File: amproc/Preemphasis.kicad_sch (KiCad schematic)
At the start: 30 parts

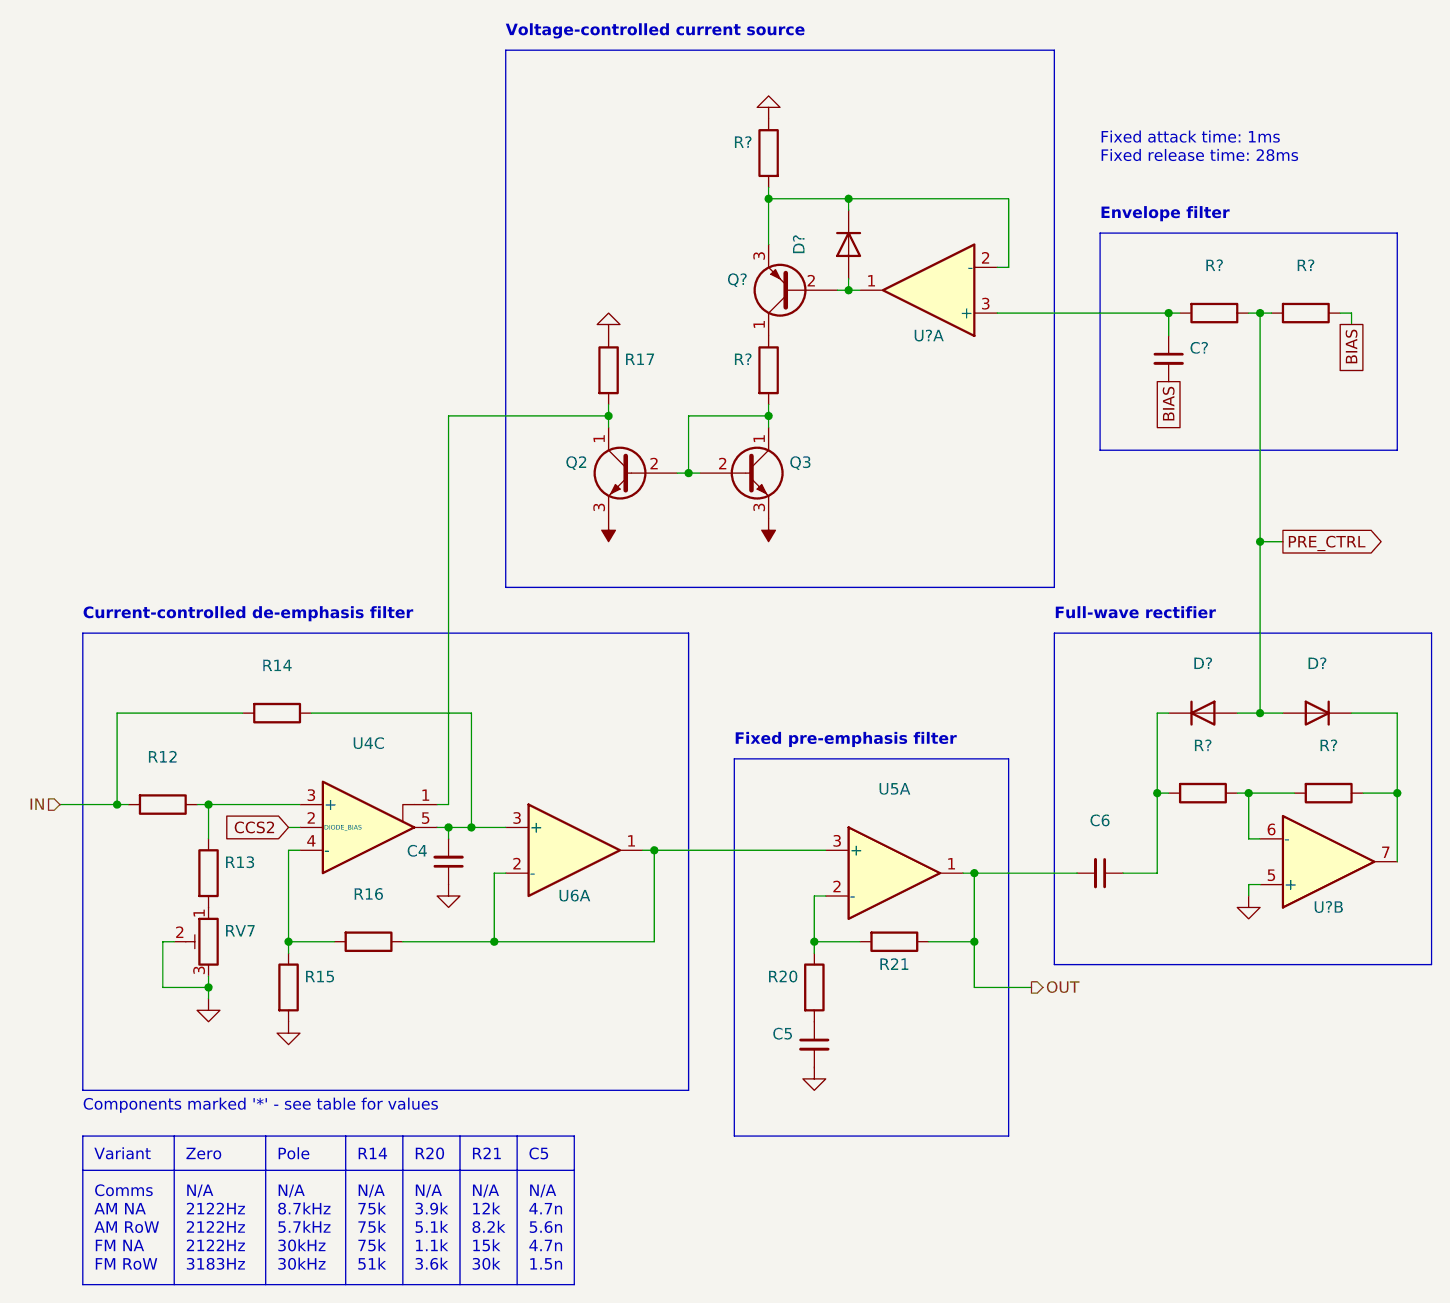
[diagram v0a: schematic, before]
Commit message: Fix U8, U9 pinouts
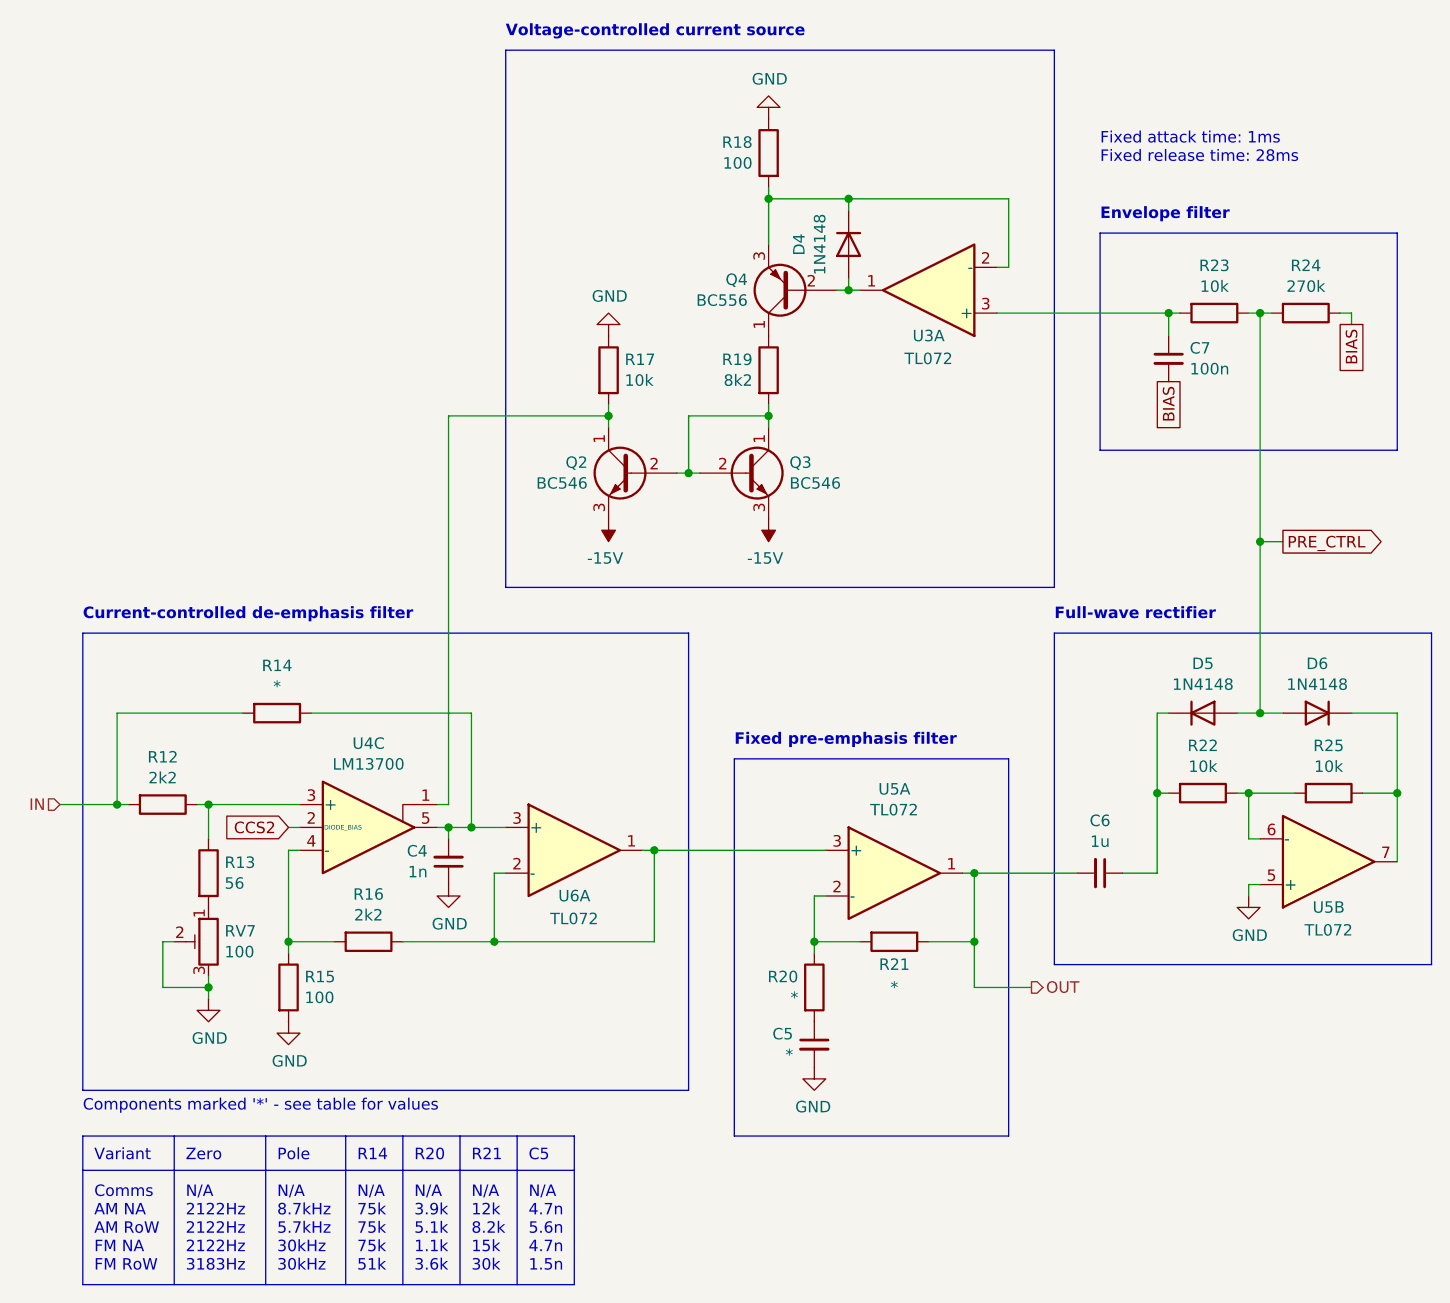
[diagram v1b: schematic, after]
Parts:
- C4: value (none) -> 1n; footprint (none) -> Capacitors_THT:C_Rect_L7.2mm_W2.5mm_P5.00mm_FKS2_FKP2_MKS2_MKP2
- C5: value (none) -> *; footprint (none) -> Capacitors_THT:C_Rect_L7.2mm_W2.5mm_P5.00mm_FKS2_FKP2_MKS2_MKP2
- C6: value (none) -> 1u; footprint (none) -> Capacitors_THT:C_Rect_L7.2mm_W5.5mm_P5.00mm_FKS2_FKP2_MKS2_MKP2
- C7: renamed from C?; value (none) -> 100n; footprint (none) -> Capacitors_THT:C_Rect_L7.2mm_W2.5mm_P5.00mm_FKS2_FKP2_MKS2_MKP2
- D4, D5, D6: renamed from D?; value (none) -> 1N4148; footprint (none) -> Diodes_THT:D_DO-35_SOD27_P7.62mm_Horizontal
- Q2, Q3: value (none) -> BC546; footprint (none) -> TO_SOT_Packages_THT:TO-92_Inline_Narrow_Oval
- Q4: renamed from Q?; value (none) -> BC556; footprint (none) -> TO_SOT_Packages_THT:TO-92_Inline_Narrow_Oval
- R12, R16: value (none) -> 2k2; footprint (none) -> amproc:R_Axial_DIN0207_L6.3mm_D2.5mm_P7.62mm_Horizontal_FabText
- R13: value (none) -> 56; footprint (none) -> amproc:R_Axial_DIN0207_L6.3mm_D2.5mm_P7.62mm_Horizontal_FabText
- R14, R20, R21: value (none) -> *; footprint (none) -> amproc:R_Axial_DIN0207_L6.3mm_D2.5mm_P7.62mm_Horizontal_FabText
- R15: value (none) -> 100; footprint (none) -> amproc:R_Axial_DIN0207_L6.3mm_D2.5mm_P7.62mm_Horizontal_FabText
- R17: value (none) -> 10k; footprint (none) -> amproc:R_Axial_DIN0207_L6.3mm_D2.5mm_P7.62mm_Horizontal_FabText
- R18: renamed from R?; value (none) -> 100; footprint (none) -> amproc:R_Axial_DIN0207_L6.3mm_D2.5mm_P7.62mm_Horizontal_FabText
- R19: renamed from R?; value (none) -> 8k2; footprint (none) -> amproc:R_Axial_DIN0207_L6.3mm_D2.5mm_P7.62mm_Horizontal_FabText
- R22, R23, R25: renamed from R?; value (none) -> 10k; footprint (none) -> amproc:R_Axial_DIN0207_L6.3mm_D2.5mm_P7.62mm_Horizontal_FabText
- R24: renamed from R?; value (none) -> 270k; footprint (none) -> amproc:R_Axial_DIN0207_L6.3mm_D2.5mm_P7.62mm_Horizontal_FabText
- RV7: value (none) -> 100; footprint (none) -> amproc:Potentiometer_Trimmer_Bourns_3296W_FabText
- U3, U5: renamed from U?; value (none) -> TL072; footprint (none) -> Housings_DIP:DIP-8_W7.62mm_LongPads
- U4: value (none) -> LM13700; footprint (none) -> Housings_DIP:DIP-16_W7.62mm_LongPads
- U5, U6: value (none) -> TL072; footprint (none) -> Housings_DIP:DIP-8_W7.62mm_LongPads
